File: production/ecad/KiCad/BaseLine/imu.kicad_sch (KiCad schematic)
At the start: 0 parts

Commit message: IMU circuitry
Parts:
- added C7, C8: 100nF, symbol Device:C_Small
- added R3, R4: 10k, symbol Device:R_Small_US
- added U3: BMI088, BMI088:PQFN50P450X300X100-16N, symbol BMI088:BMI088
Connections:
- new net: R3.1, U3.10 (SDO2)
- new net: R4.1, U3.15 (SDO1)
- new net +3.3V: C7.1, C8.1, U3.11 (VDDIO), U3.14 (CSB1), U3.3 (VDD), U3.7 (PS)
- new net GND: C7.2, C8.2, R3.2, R4.2, U3.2 (NC), U3.4 (GNDA), U3.6 (GNDIO)
- new net SCL: U3.8 (SCL/SCK)
- new net SDA: U3.9 (SDA/SDI)
- no-connect marks 0 -> 5

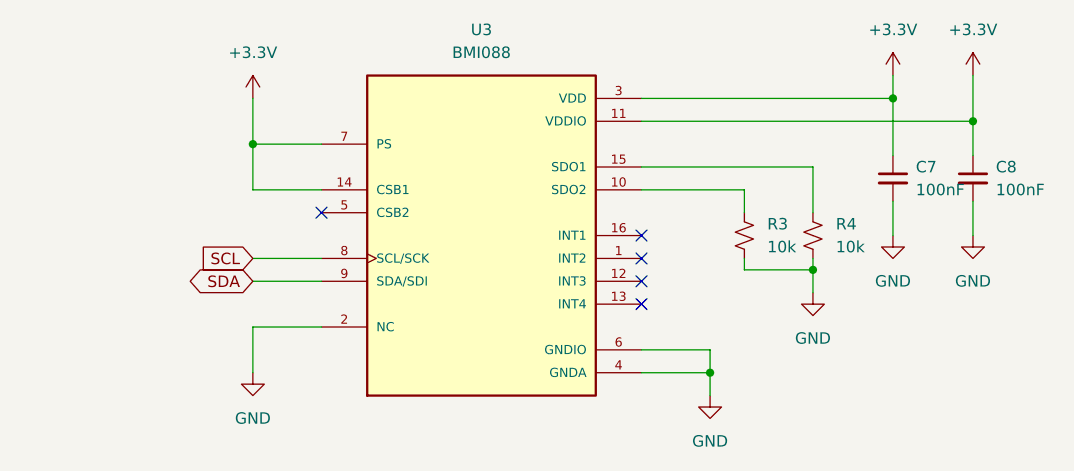
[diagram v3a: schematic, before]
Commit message: testpoints on rotary encoder & IMU
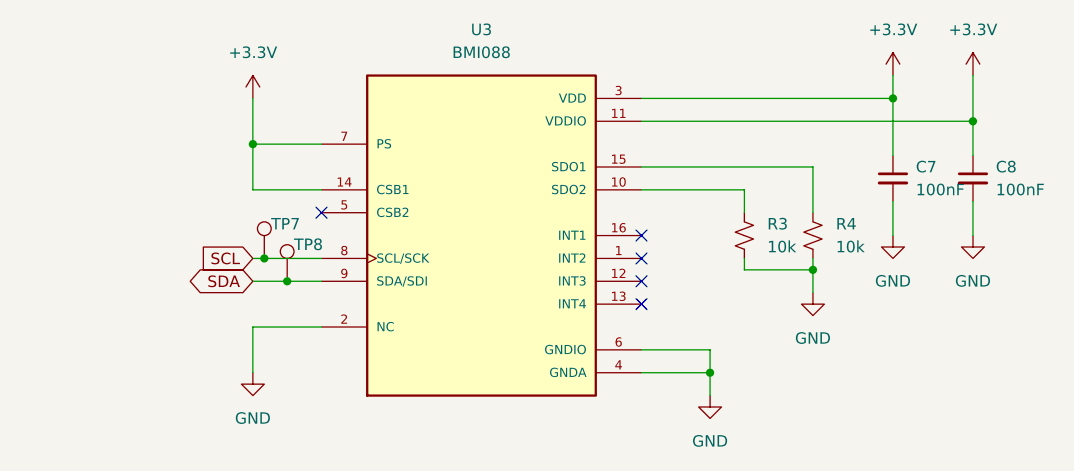
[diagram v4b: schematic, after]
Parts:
- added TP7, TP8: ~, symbol Connector:TestPoint
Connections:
- net SCL: now also TP7.1
- net SDA: now also TP8.1
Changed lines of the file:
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@@
 	(paper "A5")
+	(junction
+		(at 67.31 68.58)
+		(diameter 0)
+		(color 0 0 0 0)
+	)
 	(junction
 		(at 125.73 67.31)
@@
 	)
 	(junction
+		(at 64.77 66.04)
+		(diameter 0)
+		(color 0 0 0 0)
+	)
+	(junction
 		(at 143.51 50.8)
 		(diameter 0)
@@
 	(wire
 		(pts
+			(xy 67.31 68.58) (xy 71.12 68.58)
+		)
+		(stroke
+			(width 0)
+			(type default)
+		)
+	)
+	(wire
+		(pts
 			(xy 63.5 53.34) (xy 63.5 58.42)
 		)
@@
 	(wire
 		(pts
+			(xy 64.77 66.04) (xy 71.12 66.04)
+		)
+		(stroke
+			(width 0)
+			(type default)
+		)
+	)
+	(wire
+		(pts
 			(xy 134.62 48.26) (xy 134.62 54.61)
 		)
@@
 	(wire
 		(pts
-			(xy 63.5 68.58) (xy 71.12 68.58)
+			(xy 63.5 68.58) (xy 67.31 68.58)
 		)
 		(stroke
@@
 	(wire
 		(pts
-			(xy 63.5 66.04) (xy 71.12 66.04)
+			(xy 63.5 66.04) (xy 64.77 66.04)
 		)
 		(stroke
@@
 	)
 	(symbol
+		(lib_id "Connector:TestPoint")
+		(at 67.31 68.58 0)
+		(unit 1)
+		(exclude_from_sim no)
+		(in_bom yes)
+		(on_board yes)
+		(dnp no)
+		(property "Reference" "TP8"
+			(at 68.072 64.516 0)
+			(effects
+				(font
+					(size 1.27 1.27)
+				)
+				(justify left)
+			)
+		)
+		(property "Value" "~"
+			(at 69.85 66.548 0)
+			(effects
+				(font
+					(size 1.27 1.27)
+				)
+				(justify left)
+			)
+		)
+		(property "Footprint" ""
+			(at 72.39 68.58 0)
+			(effects
+				(font
+					(size 1.27 1.27)
+				)
+				(hide yes)
+			)
+		)
+		(property "Datasheet" "~"
+			(at 72.39 68.58 0)
+			(effects
+				(font
+					(size 1.27 1.27)
+				)
+				(hide yes)
+			)
+		)
+		(property "Description" "test point"
+			(at 67.31 68.58 0)
+			(effects
+				(font
+					(size 1.27 1.27)
+				)
+				(hide yes)
+			)
+		)
+		(pin "1"
+		)
+		(instances
+			(project "BaseLine"
+				(path "/ba9eda21-3882-41e1-8265-3d8ac781da20/68201867-5890-4998-aaba-53bdb901d337"
+					(reference "TP8")
+					(unit 1)
+				)
+			)
+		)
+	)
+	(symbol
 		(lib_id "Device:R_Small_US")
 		(at 118.11 63.5 0)
@@
 					(unit 1)
 				)
+			)
+		)
+	)
+	(symbol
+		(lib_id "Connector:TestPoint")
+		(at 64.77 66.04 0)
+		(unit 1)
+		(exclude_from_sim no)
+		(in_bom yes)
+		(on_board yes)
+		(dnp no)
+		(property "Reference" "TP7"
+			(at 65.532 62.23 0)
+			(effects
+				(font
+					(size 1.27 1.27)
+				)
+				(justify left)
+			)
+		)
+		(property "Value" "~"
+			(at 67.31 64.008 0)
+			(effects
+				(font
+					(size 1.27 1.27)
+				)
+				(justify left)
+			)
+		)
+		(property "Footprint" ""
+			(at 69.85 66.04 0)
+			(effects
+				(font
+					(size 1.27 1.27)
+				)
+				(hide yes)
+			)
+		)
+		(property "Datasheet" "~"
+			(at 69.85 66.04 0)
+			(effects
+				(font
+					(size 1.27 1.27)
+				)
+				(hide yes)
+			)
+		)
+		(property "Description" "test point"
+			(at 64.77 66.04 0)
+			(effects
+				(font
+					(size 1.27 1.27)
+				)
+				(hide yes)
+			)
+		)
+		(pin "1"
+		)
+		(instances
+			(project "BaseLine"
+				(path "/ba9eda21-3882-41e1-8265-3d8ac781da20/68201867-5890-4998-aaba-53bdb901d337"
+					(reference "TP7")
+					(unit 1)
+				)

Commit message: Changed annotations
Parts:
- renumbered C7 to C8, C8 to C9, R3 to R27, R4 to R28, TP7 to TP8, TP8 to TP9, U3 to U4
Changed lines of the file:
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@@
 		(dnp no)
 		(fields_autoplaced yes)
-		(property "Reference" "U3"
+		(property "Reference" "U4"
 			(at 88.9 40.64 0)
 			(effects
@@
 			(project ""
 				(path "/ba9eda21-3882-41e1-8265-3d8ac781da20/68201867-5890-4998-aaba-53bdb901d337"
-					(reference "U3")
+					(reference "U4")
 					(unit 1)
 				)
@@
 		(dnp no)
 		(fields_autoplaced yes)
-		(property "Reference" "C8"
+		(property "Reference" "C9"
 			(at 146.05 55.8862 0)
 			(effects
@@
 			(project "BaseLine"
 				(path "/ba9eda21-3882-41e1-8265-3d8ac781da20/68201867-5890-4998-aaba-53bdb901d337"
-					(reference "C8")
+					(reference "C9")
 					(unit 1)
 				)
@@
 		(dnp no)
 		(fields_autoplaced yes)
-		(property "Reference" "R4"
+		(property "Reference" "R28"
 			(at 128.27 62.2299 0)
 			(effects
@@
 			(project "BaseLine"
 				(path "/ba9eda21-3882-41e1-8265-3d8ac781da20/68201867-5890-4998-aaba-53bdb901d337"
-					(reference "R4")
+					(reference "R28")
 					(unit 1)
 				)
@@
 		(dnp no)
 		(fields_autoplaced yes)
-		(property "Reference" "#PWR016"
+		(property "Reference" "#PWR033"
 			(at 143.51 49.53 0)
 			(effects
@@
 			(project "BaseLine"
 				(path "/ba9eda21-3882-41e1-8265-3d8ac781da20/68201867-5890-4998-aaba-53bdb901d337"
-					(reference "#PWR016")
+					(reference "#PWR033")
 					(unit 1)
 				)
@@
 		(on_board yes)
 		(dnp no)
-		(property "Reference" "TP8"
+		(property "Reference" "TP9"
 			(at 68.072 64.516 0)
 			(effects
@@
 			(project "BaseLine"
 				(path "/ba9eda21-3882-41e1-8265-3d8ac781da20/68201867-5890-4998-aaba-53bdb901d337"
-					(reference "TP8")
+					(reference "TP9")
 					(unit 1)
 				)
@@
 		(dnp no)
 		(fields_autoplaced yes)
-		(property "Reference" "R3"
+		(property "Reference" "R27"
 			(at 120.65 62.2299 0)
 			(effects
@@
 			(project ""
 				(path "/ba9eda21-3882-41e1-8265-3d8ac781da20/68201867-5890-4998-aaba-53bdb901d337"
-					(reference "R3")
+					(reference "R27")
 					(unit 1)
 				)
@@
 		(dnp no)
 		(fields_autoplaced yes)
-		(property "Reference" "#PWR014"
+		(property "Reference" "#PWR029"
 			(at 114.3 87.63 0)
 			(effects
@@
 			(project "BaseLine"
 				(path "/ba9eda21-3882-41e1-8265-3d8ac781da20/68201867-5890-4998-aaba-53bdb901d337"
-					(reference "#PWR014")
+					(reference "#PWR029")
 					(unit 1)
 				)
@@
 		(dnp no)
 		(fields_autoplaced yes)
-		(property "Reference" "#PWR015"
+		(property "Reference" "#PWR030"
 			(at 125.73 76.2 0)
 			(effects
@@
 			(project "BaseLine"
 				(path "/ba9eda21-3882-41e1-8265-3d8ac781da20/68201867-5890-4998-aaba-53bdb901d337"
-					(reference "#PWR015")
+					(reference "#PWR030")
 					(unit 1)
 				)
@@
 		(dnp no)
 		(fields_autoplaced yes)
-		(property "Reference" "#PWR010"
+		(property "Reference" "#PWR028"
 			(at 63.5 85.09 0)
 			(effects
@@
 			(project ""
 				(path "/ba9eda21-3882-41e1-8265-3d8ac781da20/68201867-5890-4998-aaba-53bdb901d337"
-					(reference "#PWR010")
+					(reference "#PWR028")
 					(unit 1)
 				)
@@
 		(dnp no)
 		(fields_autoplaced yes)
-		(property "Reference" "#PWR017"
+		(property "Reference" "#PWR032"
 			(at 134.62 69.85 0)
 			(effects
@@
 			(project "BaseLine"
 				(path "/ba9eda21-3882-41e1-8265-3d8ac781da20/68201867-5890-4998-aaba-53bdb901d337"
-					(reference "#PWR017")
+					(reference "#PWR032")
 					(unit 1)
 				)
@@
 		(dnp no)
 		(fields_autoplaced yes)
-		(property "Reference" "#PWR013"
+		(property "Reference" "#PWR027"
 			(at 63.5 52.07 0)
 			(effects
@@
 			(project ""
 				(path "/ba9eda21-3882-41e1-8265-3d8ac781da20/68201867-5890-4998-aaba-53bdb901d337"
-					(reference "#PWR013")
+					(reference "#PWR027")
 					(unit 1)
 				)
@@
 		(dnp no)
 		(fields_autoplaced yes)
-		(property "Reference" "C7"
+		(property "Reference" "C8"
 			(at 137.16 55.8862 0)
 			(effects
@@
 			(project ""
 				(path "/ba9eda21-3882-41e1-8265-3d8ac781da20/68201867-5890-4998-aaba-53bdb901d337"
-					(reference "C7")
+					(reference "C8")
 					(unit 1)
 				)
@@
 		(dnp no)
 		(fields_autoplaced yes)
-		(property "Reference" "#PWR018"
+		(property "Reference" "#PWR034"
 			(at 143.51 69.85 0)
 			(effects
@@
 			(project "BaseLine"
 				(path "/ba9eda21-3882-41e1-8265-3d8ac781da20/68201867-5890-4998-aaba-53bdb901d337"
-					(reference "#PWR018")
+					(reference "#PWR034")
 					(unit 1)
 				)
@@
 		(dnp no)
 		(fields_autoplaced yes)
-		(property "Reference" "#PWR019"
+		(property "Reference" "#PWR031"
 			(at 134.62 49.53 0)
 			(effects
@@
 			(project "BaseLine"
 				(path "/ba9eda21-3882-41e1-8265-3d8ac781da20/68201867-5890-4998-aaba-53bdb901d337"
-					(reference "#PWR019")
+					(reference "#PWR031")
 					(unit 1)
 				)
@@
 		(on_board yes)
 		(dnp no)
-		(property "Reference" "TP7"
+		(property "Reference" "TP8"
 			(at 65.532 62.23 0)
 			(effects
@@
 			(project "BaseLine"
 				(path "/ba9eda21-3882-41e1-8265-3d8ac781da20/68201867-5890-4998-aaba-53bdb901d337"
-					(reference "TP7")
-					(unit 1)
-				)
+					(reference "TP8")
+					(unit 1)
+				)

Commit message: More updated annotations and stuff
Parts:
- renumbered R27 to R30, R28 to R31
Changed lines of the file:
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@@
 		(dnp no)
 		(fields_autoplaced yes)
-		(property "Reference" "R28"
+		(property "Reference" "R31"
 			(at 128.27 62.2299 0)
 			(effects
@@
 			(project "BaseLine"
 				(path "/ba9eda21-3882-41e1-8265-3d8ac781da20/68201867-5890-4998-aaba-53bdb901d337"
-					(reference "R28")
+					(reference "R31")
 					(unit 1)
 				)
@@
 		(dnp no)
 		(fields_autoplaced yes)
-		(property "Reference" "R27"
+		(property "Reference" "R30"
 			(at 120.65 62.2299 0)
 			(effects
@@
 			(project ""
 				(path "/ba9eda21-3882-41e1-8265-3d8ac781da20/68201867-5890-4998-aaba-53bdb901d337"
-					(reference "R27")
-					(unit 1)
-				)
+					(reference "R30")
+					(unit 1)
+				)

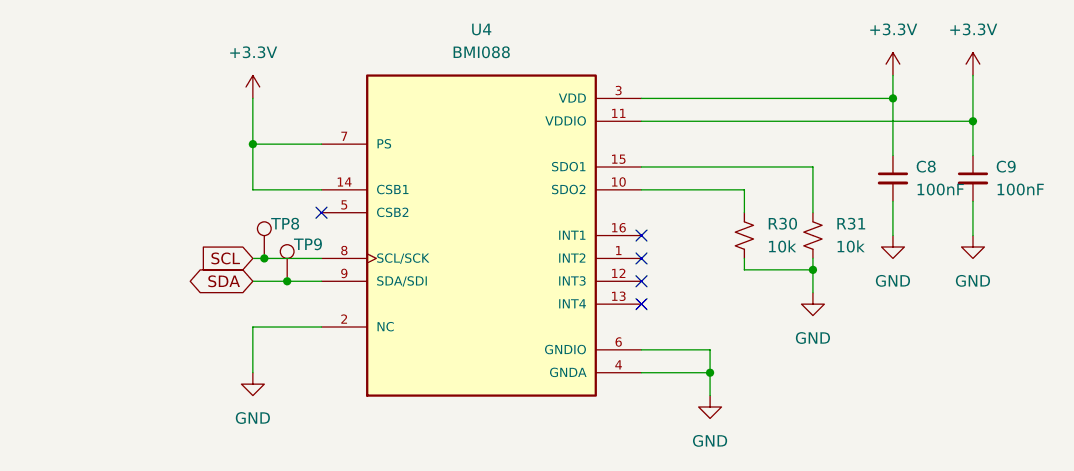
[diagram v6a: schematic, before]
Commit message: add connector IMU
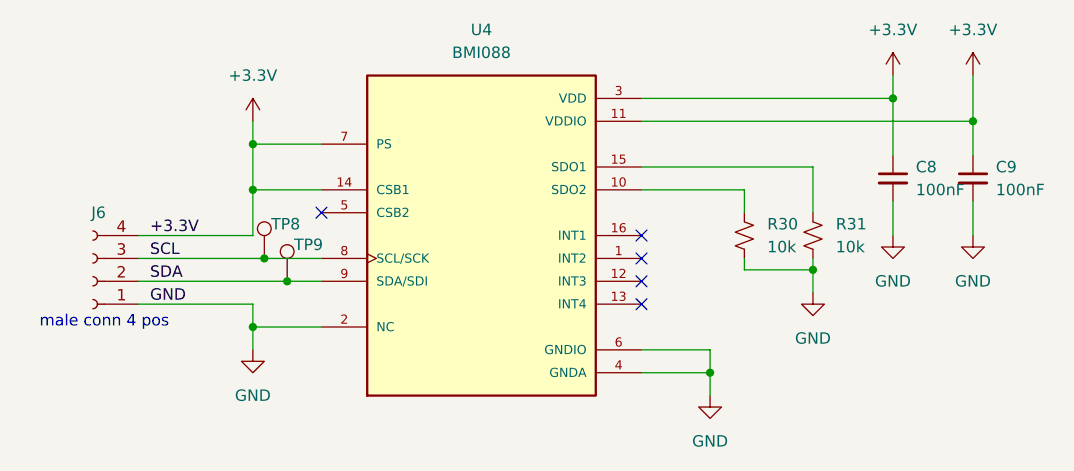
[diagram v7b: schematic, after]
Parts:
- added J6: Conn_01x04_Socket, Connector_JST:JST_EH_B4B-EH-A_1x04_P2.50mm_Vertical, symbol Connector:Conn_01x04_Socket
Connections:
- net +3.3V: now also J6.4 (Pin_4)
- net GND: now also J6.1 (Pin_1)
- net SCL: now also J6.3 (Pin_3)
- net SDA: now also J6.2 (Pin_2)
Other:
- note added: "male conn 4 pos"
